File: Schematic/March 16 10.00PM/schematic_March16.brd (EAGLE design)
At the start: 179.6 x 161.1 mm, 315 parts, among them CON1 UBC05V128-B0C04D, IC10 TL084D, IC3 TL084D, IC4 TL084D, IC5 TL084D, IC6 TL084D, IC7 TL084D, IC8 TL084D, IC9 TL084D, Q2 BC557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

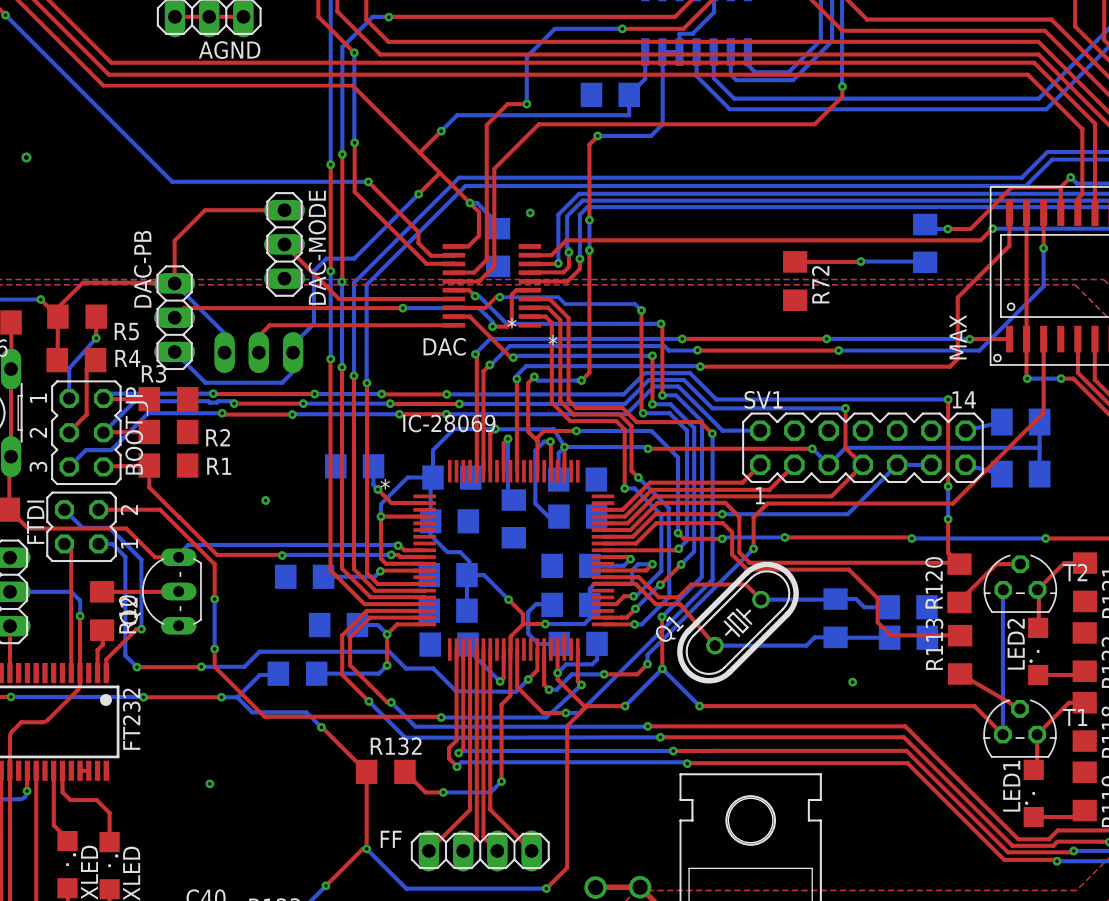
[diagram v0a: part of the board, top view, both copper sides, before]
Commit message: Minor corrections in DAC connections, decoupling placed for DAC
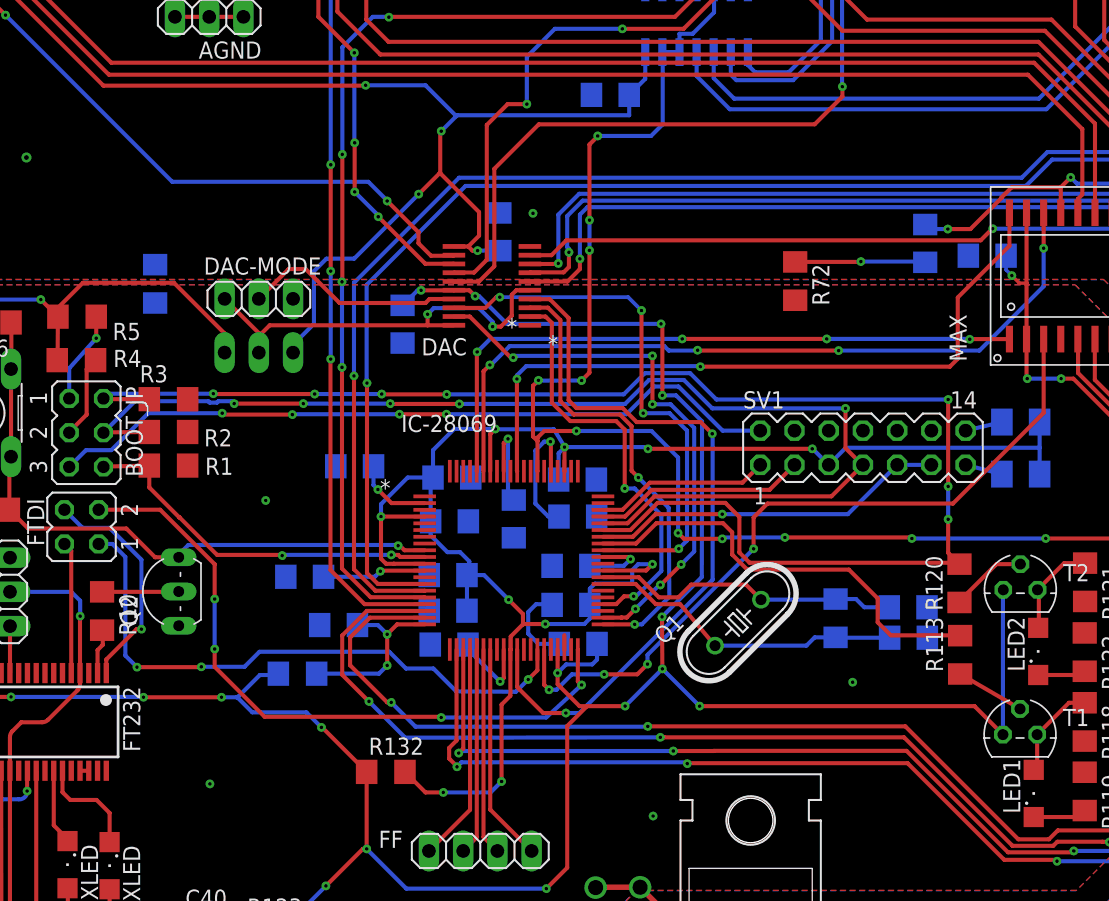
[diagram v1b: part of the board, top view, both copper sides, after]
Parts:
- removed DAC-PB: (no value), pinhead:1X03
- added C46, C47: 1uF, rcl:C1206
- added R135: 0, rcl:R1206
- moved C36 36.3 mm to (88.2, -15.5), turned to 0 degrees
- moved DAC-MODE 4.47 mm to (34.2, -18.7), turned to 0 degrees
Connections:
- removed net PREBAR: DAC-PB.2, DAC.5
- net +3V3: now also C47.1; no longer DAC-MODE.1, DAC-PB.1
- net +5V: now also C46.1; no longer DAC-PB.3
- net AGND: now also C46.2, R135.1
- net DVDD: now also DAC-MODE.1, DAC.5
- net GND: now also C47.2, R135.2
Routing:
- net PREBAR: track 29.7 -> 0.00 mm, vias 2 -> 0
- net DVDD: track 16.0 -> 31.3 mm, vias 0 -> 2
- net +5V: track 1001.0 -> 992.1 mm, vias 38 -> 40
- net +3V3: track 583.2 -> 575.5 mm, vias 41 -> 42
- net ?????: track 14.2 -> 16.6 mm
- net INT_CONTROL: track 118.3 -> 117.5 mm
- net GND: vias 4 -> 5
- net DACO2: vias 3 -> 5
